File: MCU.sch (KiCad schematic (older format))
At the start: 25 parts, among them J2 JTAG, SW1 Reset, U6 STM32F303RETx, U7 MAX7375AXR805

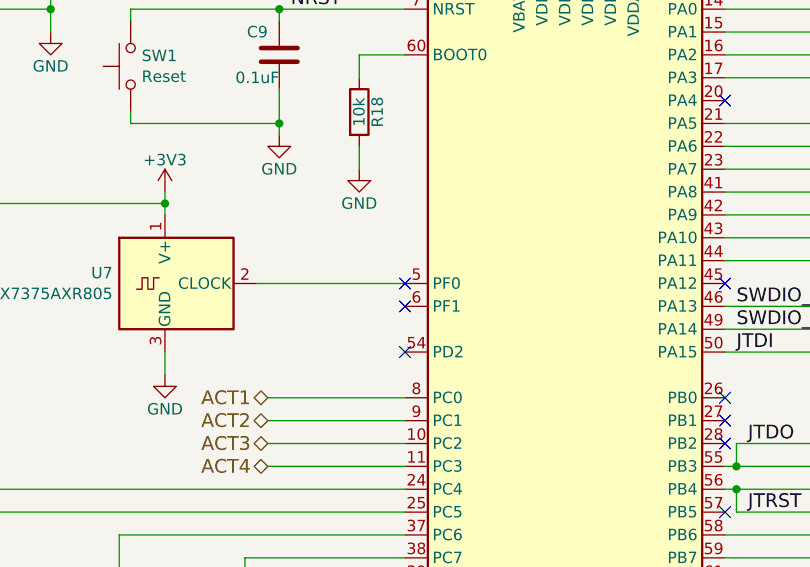
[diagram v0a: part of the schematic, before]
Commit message: All ERC errors gone
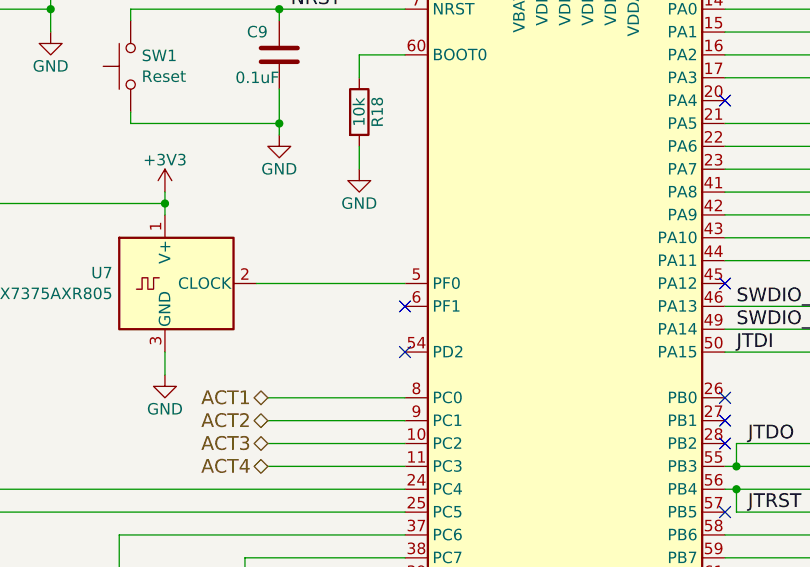
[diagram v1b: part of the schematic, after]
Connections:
- no-connect marks 18 -> 17
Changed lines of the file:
@@
 NoConn ~ 6400 4250
 NoConn ~ 6400 3650
-NoConn ~ 5000 3650
 NoConn ~ 5000 3750
 NoConn ~ 5000 3950

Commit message: Updated pinmap Added USART3 for external communication
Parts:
- removed D3, D4: BAT54S, Package_TO_SOT_SMD:SOT-23, symbol Diode:BAT54S
- removed J2: JTAG, Connector_PinHeader_1.27mm:PinHeader_2x04_P1.27mm_Vertical_SMD, symbol Connector_Generic:Conn_02x04_Odd_Even
- added J2: JTAG, Connector_PinHeader_1.27mm:PinHeader_2x05_P1.27mm_Vertical_SMD, symbol Connector_Generic:Conn_02x05_Odd_Even
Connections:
- net labels added: USART3_RX, USART3_TX
- net labels removed: ADC3, ADC4
- wire segments 156 -> 146
- no-connect marks 17 -> 15
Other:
- moved on the sheet: D5, D6, D7, D8, R14, R15, R16, R17

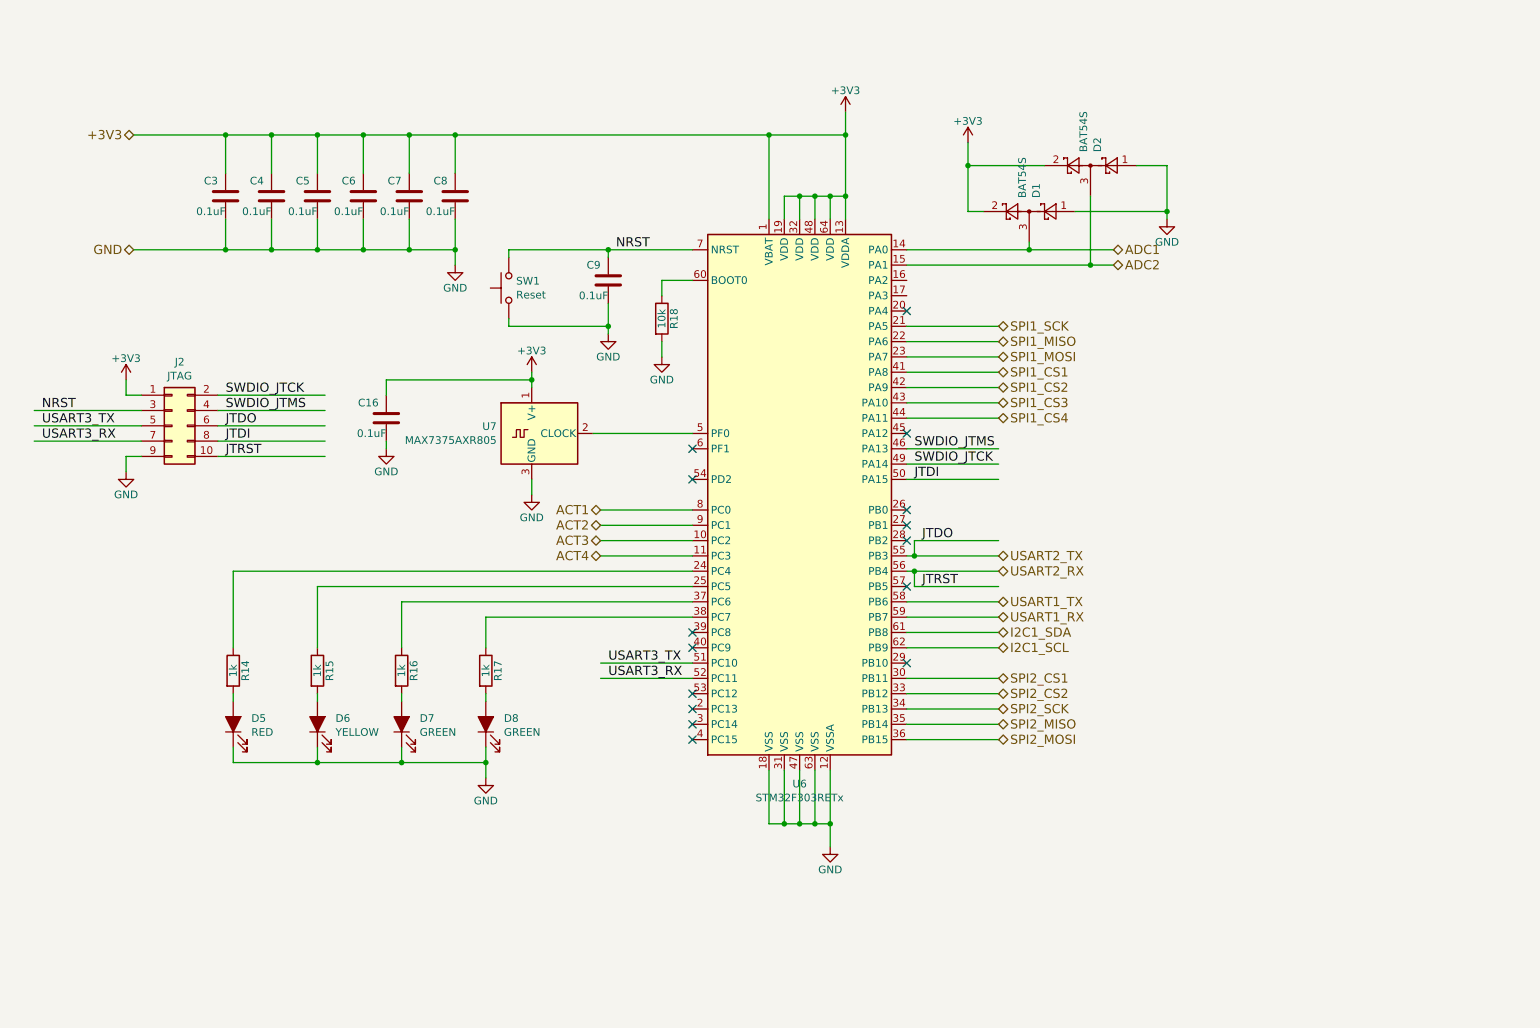
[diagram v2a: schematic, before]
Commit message: Cleaned up libraries Changed ADXL345 footprint
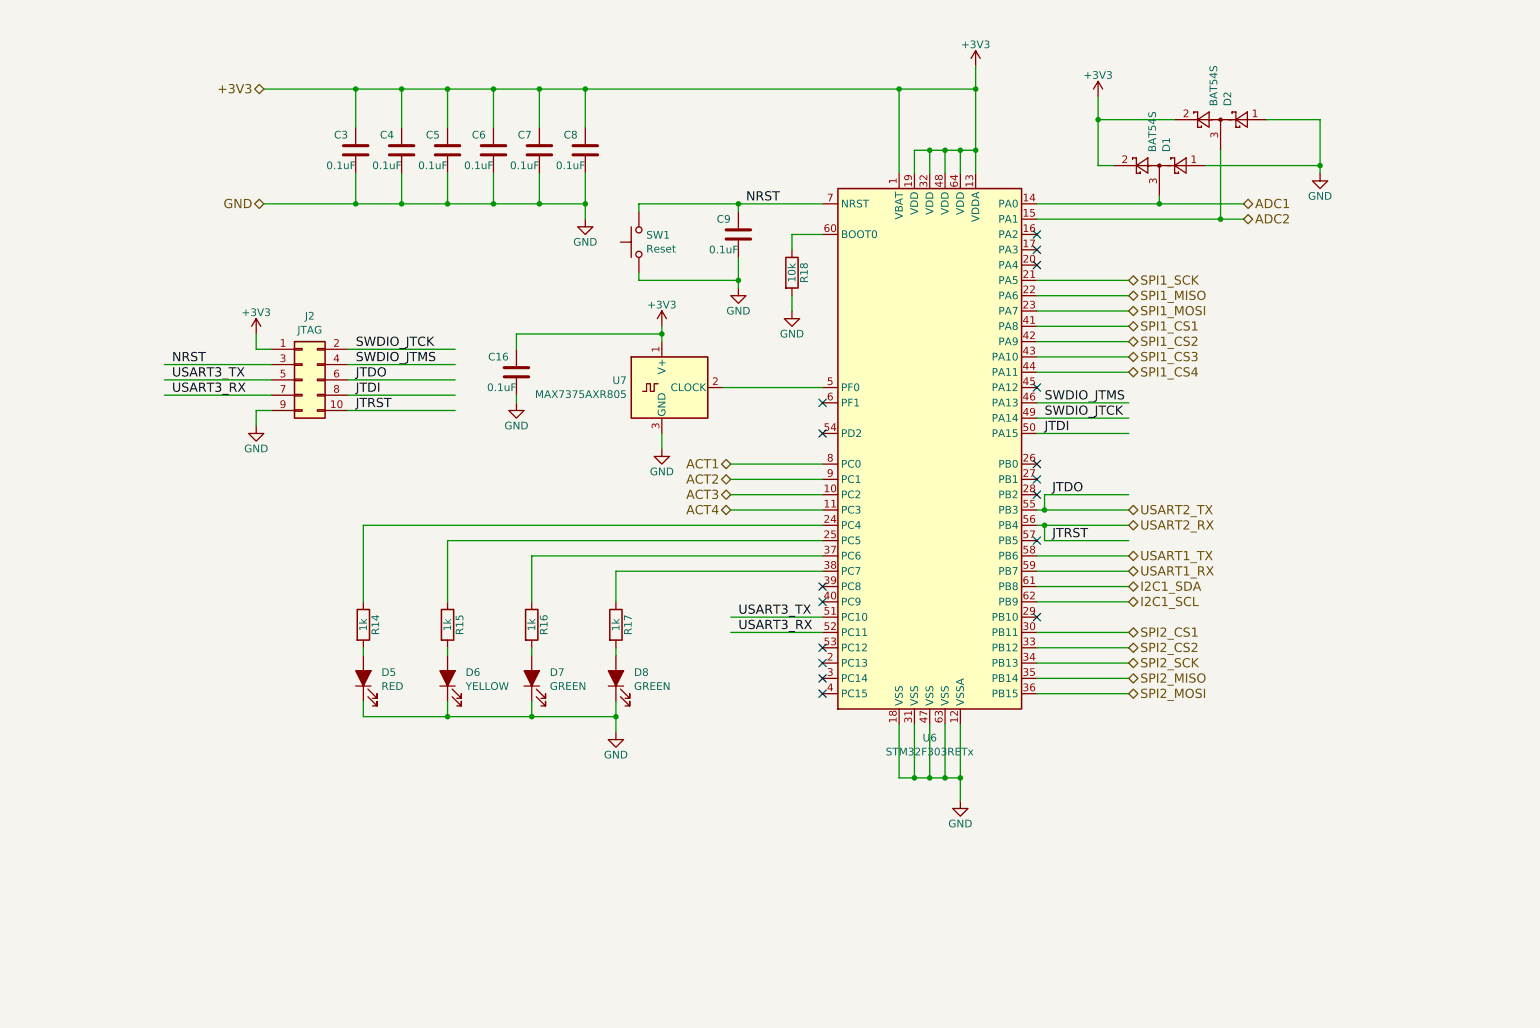
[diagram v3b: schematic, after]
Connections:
- no-connect marks 15 -> 17
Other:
- moved on the sheet: C16, C3, C4, C5, C6, C7, C8, C9, D1, D2, D5, D6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

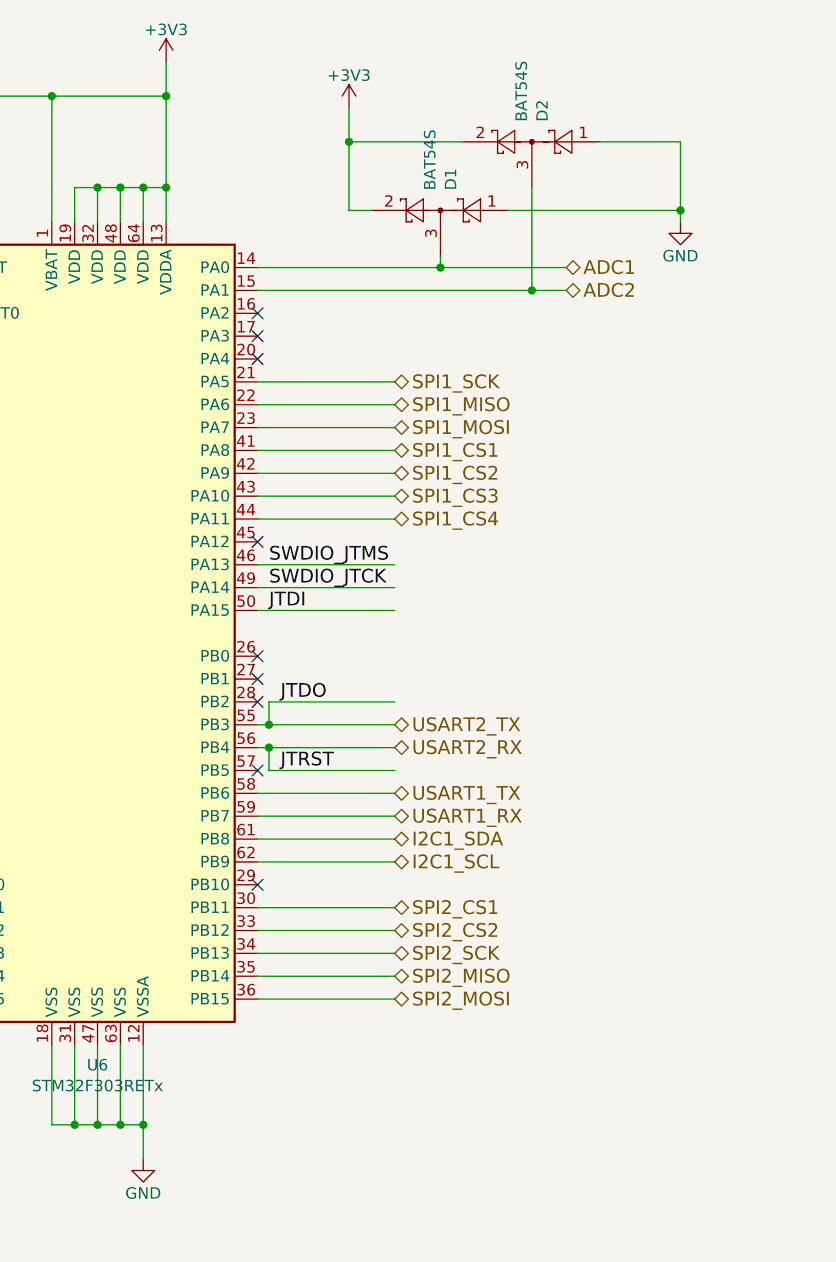
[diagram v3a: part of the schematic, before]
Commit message: Adding test points
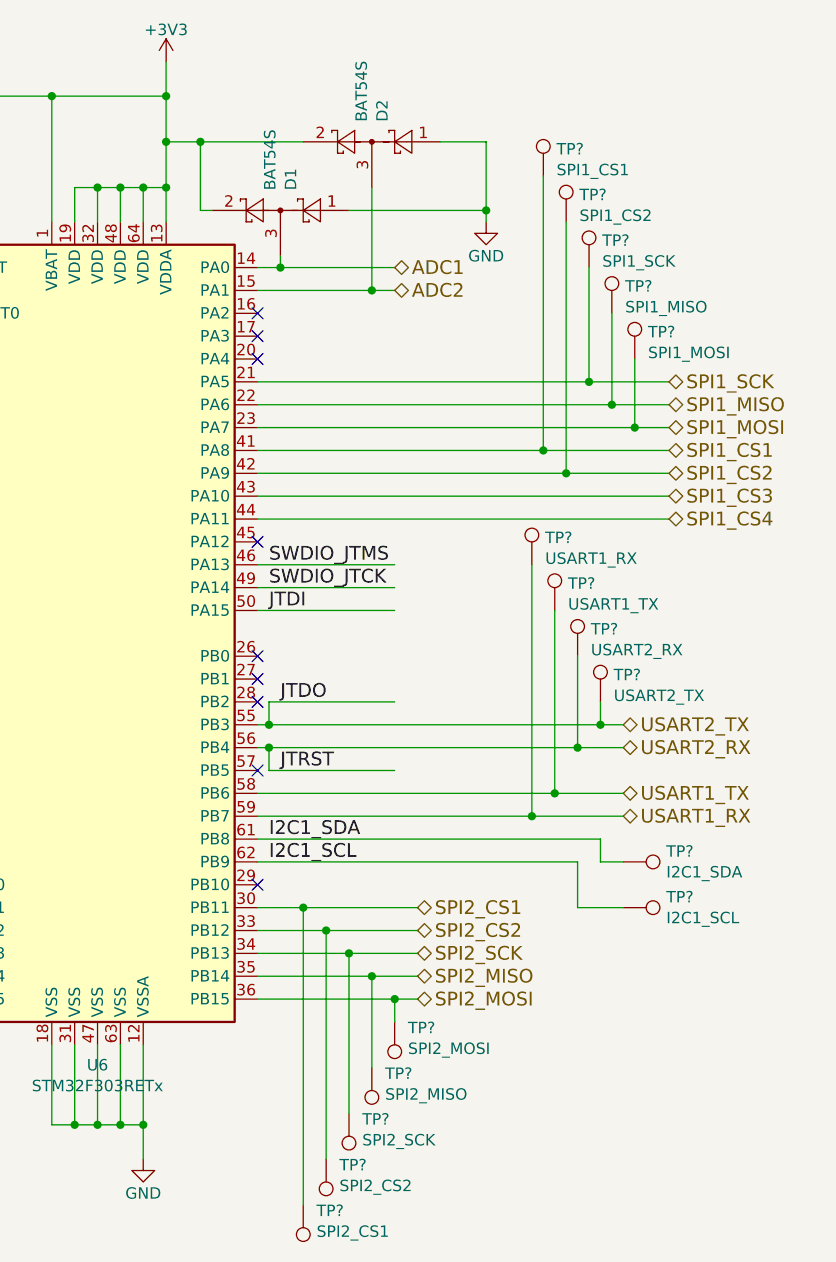
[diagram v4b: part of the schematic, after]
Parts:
- added TP?: USART1_RX, TestPoint:TestPoint_Pad_D1.0mm, symbol Connector:TestPoint
- added TP?: USART1_TX, TestPoint:TestPoint_Pad_D1.0mm, symbol Connector:TestPoint
- added TP?: USART2_RX, TestPoint:TestPoint_Pad_D1.0mm, symbol Connector:TestPoint
- added TP?: USART2_TX, TestPoint:TestPoint_Pad_D1.0mm, symbol Connector:TestPoint
- added TP?: I2C1_SDA, TestPoint:TestPoint_Pad_D1.0mm, symbol Connector:TestPoint
- added TP?: I2C1_SCL, TestPoint:TestPoint_Pad_D1.0mm, symbol Connector:TestPoint
- added TP?: SPI2_MISO, TestPoint:TestPoint_Pad_D1.0mm, symbol Connector:TestPoint
- added TP?: SPI2_MOSI, TestPoint:TestPoint_Pad_D1.0mm, symbol Connector:TestPoint
- added TP?: SPI2_SCK, TestPoint:TestPoint_Pad_D1.0mm, symbol Connector:TestPoint
- added TP?: SPI2_CS2, TestPoint:TestPoint_Pad_D1.0mm, symbol Connector:TestPoint
- added TP?: SPI2_CS1, TestPoint:TestPoint_Pad_D1.0mm, symbol Connector:TestPoint
- added TP?: SPI1_MISO, TestPoint:TestPoint_Pad_D1.0mm, symbol Connector:TestPoint
- added TP?: SPI1_MOSI, TestPoint:TestPoint_Pad_D1.0mm, symbol Connector:TestPoint
- added TP?: SPI1_SCK, TestPoint:TestPoint_Pad_D1.0mm, symbol Connector:TestPoint
- added TP?: SPI1_CS2, TestPoint:TestPoint_Pad_D1.0mm, symbol Connector:TestPoint
- added TP?: SPI1_CS1, TestPoint:TestPoint_Pad_D1.0mm, symbol Connector:TestPoint
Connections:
- wire segments 146 -> 179
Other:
- moved on the sheet: D1, D2

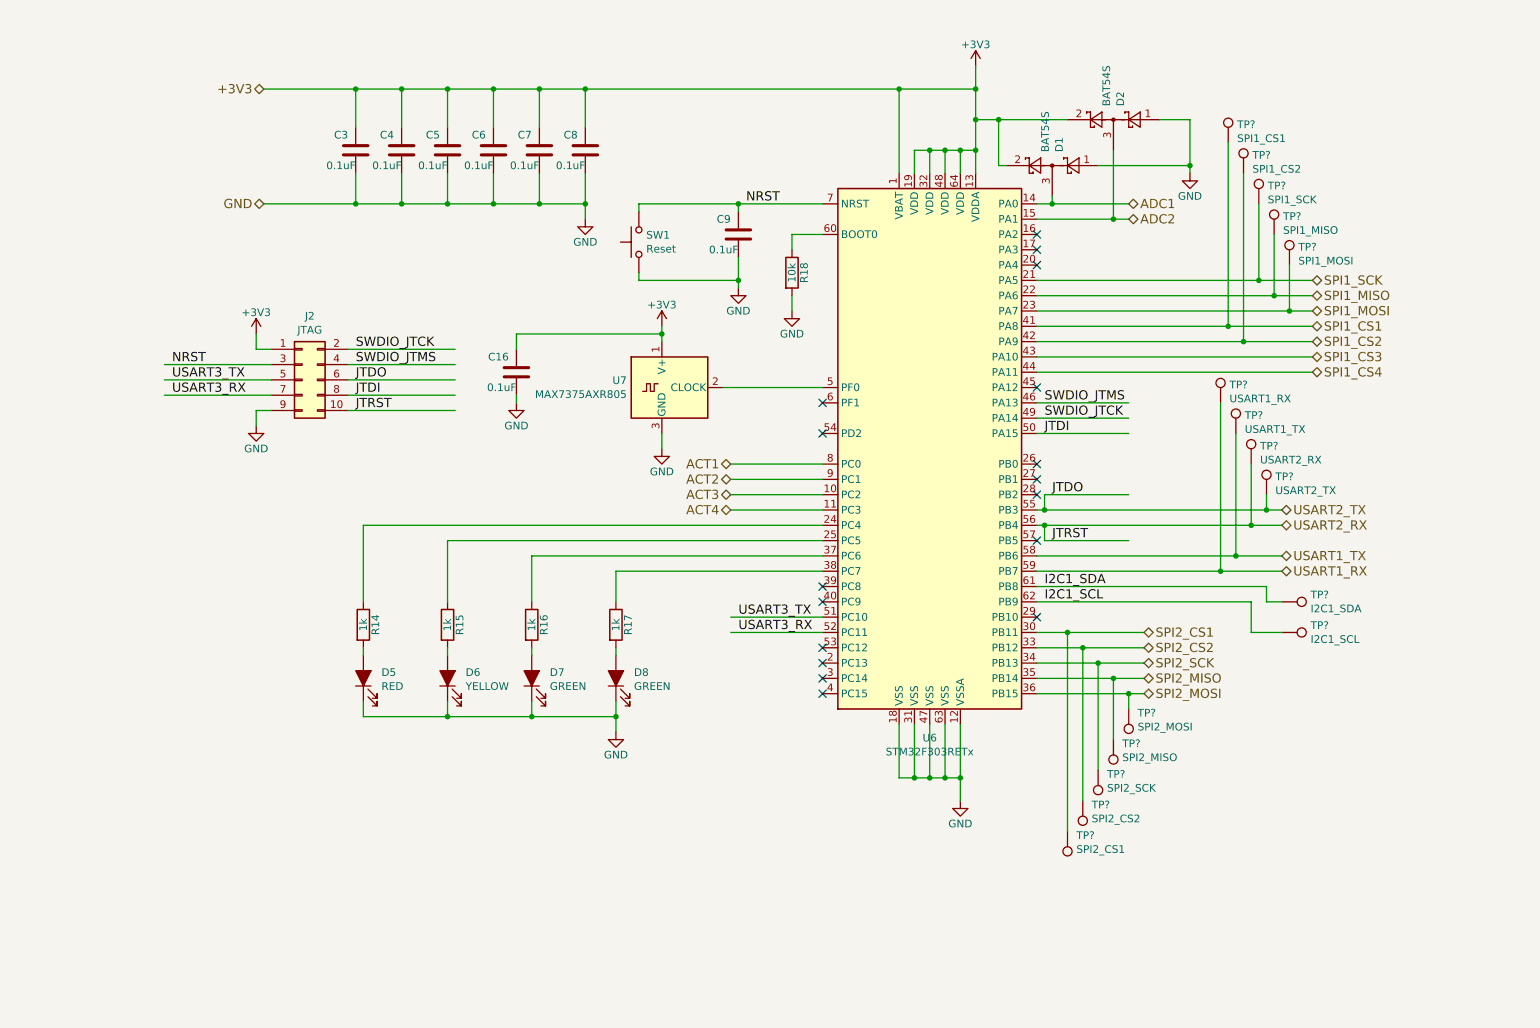
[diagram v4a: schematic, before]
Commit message: Finished adding test points Schematic annotated
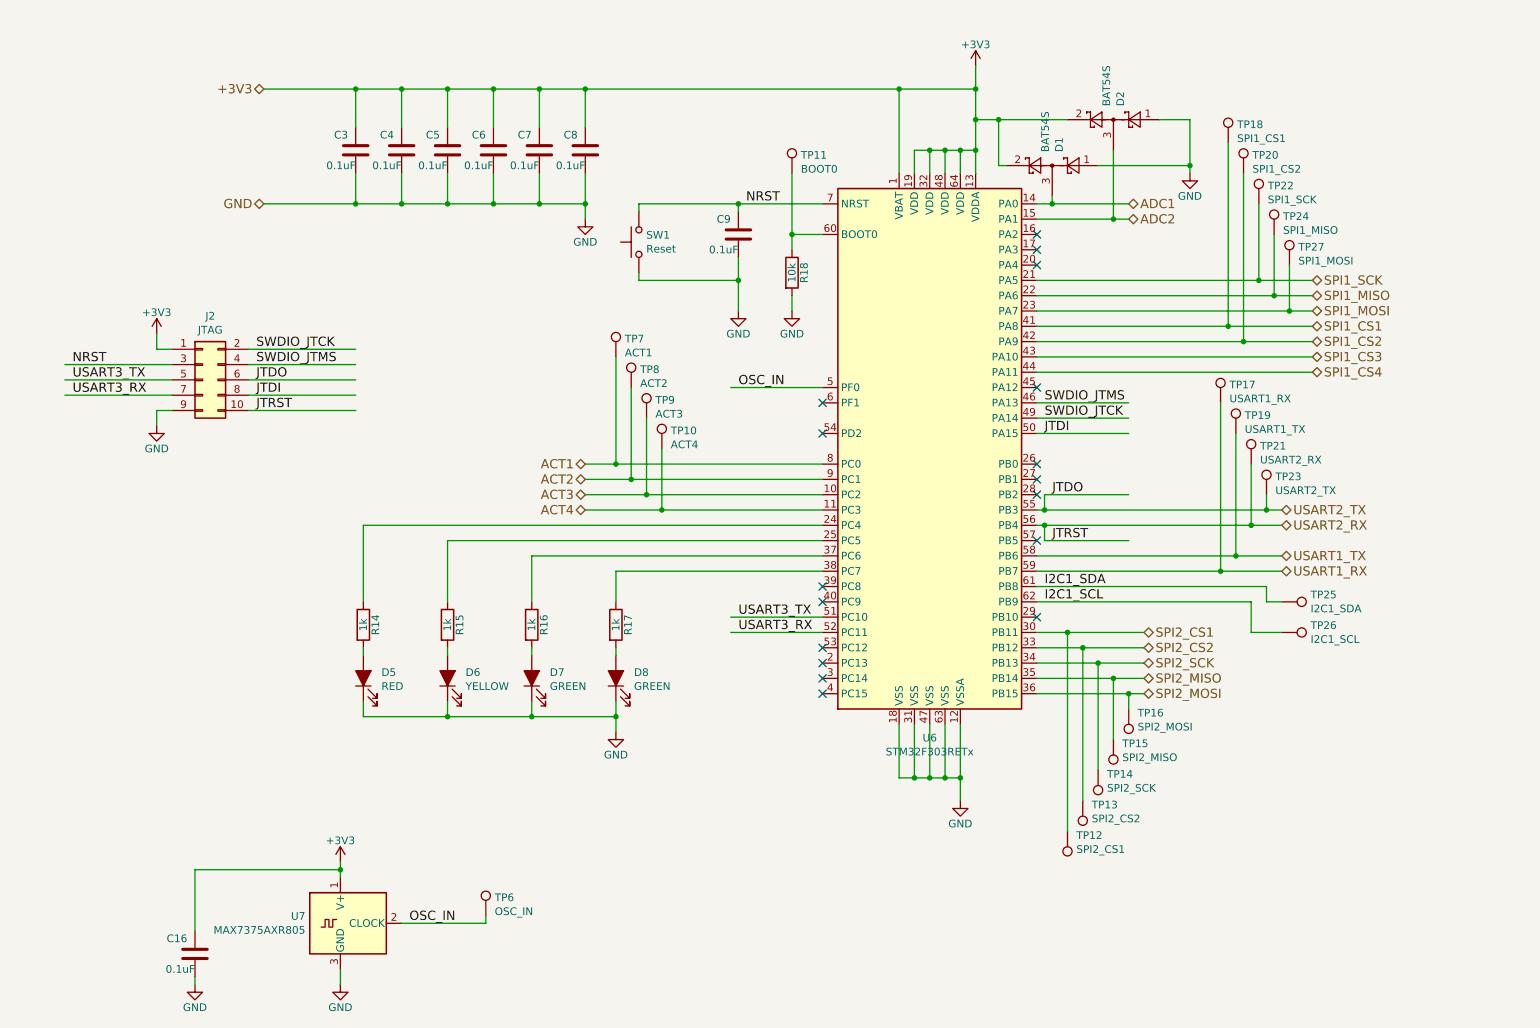
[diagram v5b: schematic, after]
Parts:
- added TP10: ACT4, TestPoint:TestPoint_Pad_D1.0mm, symbol Connector:TestPoint
- added TP11: BOOT0, TestPoint:TestPoint_Pad_D1.0mm, symbol Connector:TestPoint
- added TP6: OSC_IN, TestPoint:TestPoint_Pad_D1.0mm, symbol Connector:TestPoint
- added TP7: ACT1, TestPoint:TestPoint_Pad_D1.0mm, symbol Connector:TestPoint
- added TP8: ACT2, TestPoint:TestPoint_Pad_D1.0mm, symbol Connector:TestPoint
- added TP9: ACT3, TestPoint:TestPoint_Pad_D1.0mm, symbol Connector:TestPoint
- gave numbers to parts that had none: 16
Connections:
- net labels added: OSC_IN
- wire segments 179 -> 190
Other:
- moved on the sheet: C16, J2, U7
